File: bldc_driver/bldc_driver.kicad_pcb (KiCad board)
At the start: 2 copper layers, 46.4 x 26.5 mm, 81 parts, among them J1 I2C 1, J2 AVR-ISP-6, Q1 PSMN0R925YLC, Q2 PSMN0R925YLC, Q3 PSMN0R925YLC, Q4 PSMN0R925YLC, Q5 PSMN0R925YLC, Q6 PSMN0R925YLC, U1 ATmega328PB-AU, U2 INA199C2, U3 MIC4609

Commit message: added vias and things for grounding
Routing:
- net GND: vias 21 -> 53

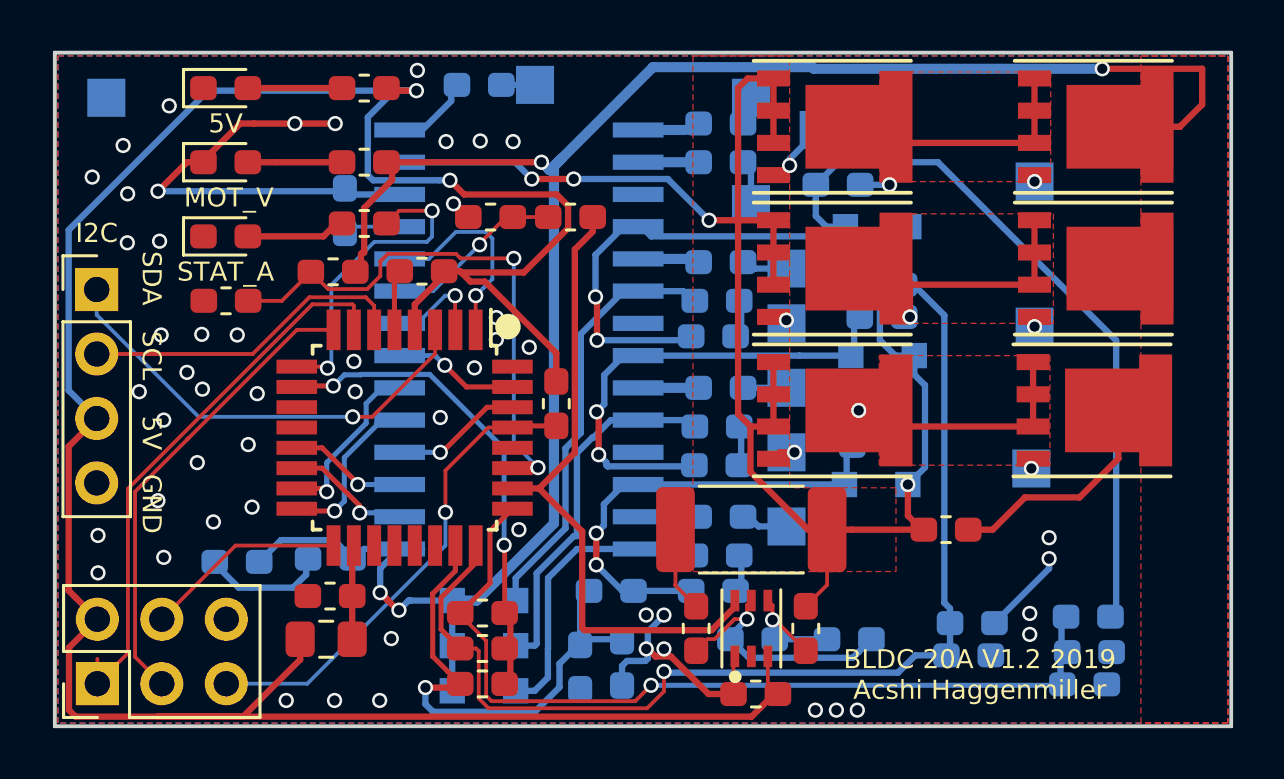
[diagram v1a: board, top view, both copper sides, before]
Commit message: redo of pcb for atmel micro at 5V to avoid emi problems resetting the old arm. initial conversion of code
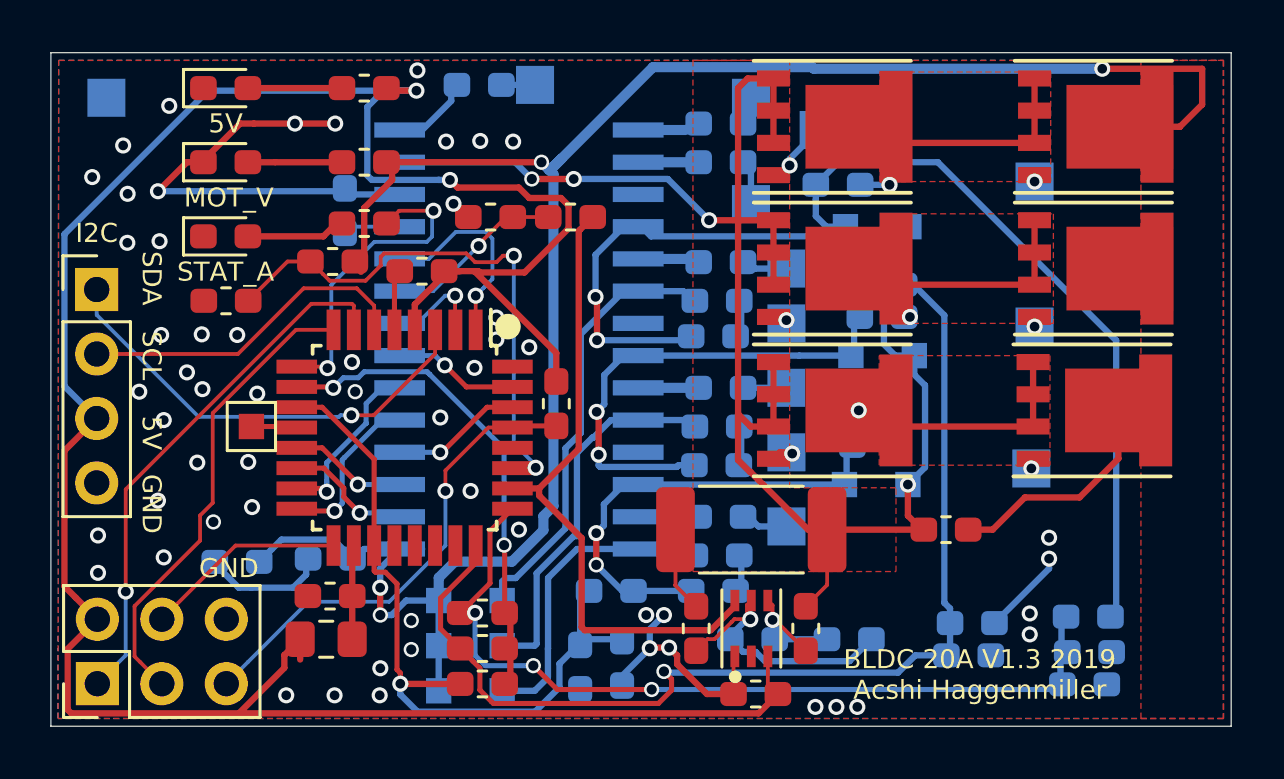
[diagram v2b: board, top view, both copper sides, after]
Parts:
- added REF**: TestPoint_Pad_1.5x1.5mm, TestPoint:TestPoint_Pad_1.5x1.5mm, F.Cu at (129.0, 87.1)
- moved D7 0.53 mm to (137.7, 94.0)
- moved D8 0.53 mm to (137.7, 95.8)
- moved D9 0.53 mm to (137.7, 97.5)
- moved R29 0.41 mm to (132.2, 80.6)
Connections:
- net /bldc_unit1/CURRENT renamed /CURRENT
- net /bldc_unit1/ENABLE renamed /ENABLE
- net /bldc_unit1/IN_HA renamed /HA
- net /bldc_unit1/IN_HB renamed /HB
- net /bldc_unit1/IN_HC renamed /HC
- net /bldc_unit1/IN_LA renamed /LA
- net /bldc_unit1/IN_LB renamed /LB
- net /bldc_unit1/IN_LC renamed /LC
- net /bldc_unit1/MOTOR_B renamed /MOTOR_B
- net /bldc_unit1/MOTOR_C renamed /MOTOR_C
- net /bldc_unit1/~FAULT renamed /~FAULT
- net Net-(R29-Pad2) renamed /V_MOT
- net Net-(U1-Pad22) renamed /TRIGGER2
- C17 pad 1: /bldc_unit1/MOTOR_A -> /MOTOR_A
- R23 pad 1: /bldc_unit1/MOTOR_A -> /MOTOR_A
- R26 pad 2: /bldc_unit1/MOTOR_A -> /MOTOR_A
- R5 pad 2: /bldc_unit1/MOTOR_A -> /MOTOR_A
- U1 pad 11: Net-(U1-Pad11) -> /MOTOR_A
- U1 pad 12: Net-(U1-Pad12) -> /TRIGGER
- U1 pad 19: Net-(U1-Pad19) -> /MOTOR_A
- U1 pad 23: /bldc_unit1/MOTOR_A -> Net-(U1-Pad23)
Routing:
- net /MOTOR_A: track 0.00 -> 29.7 mm, vias 0 -> 1
- net /bldc_unit1/MOTOR_A: track 20.2 -> 0.00 mm, vias 1 -> 0
- net /+5V: track 104.3 -> 102.0 mm
- net /TRIGGER: track 0.00 -> 1.86 mm
- net /MISO: track 22.5 -> 21.6 mm, vias 1 -> 2
- net /MOTOR_C: track 34.8 -> 34.1 mm, vias 1 -> 3
- net /bldc_unit1/MOTOR_SHUNT: track 66.7 -> 67.3 mm
- net GND: track 44.8 -> 44.3 mm, vias 53 -> 56
- net /+V_MOTOR: track 91.2 -> 91.7 mm
- net Net-(C15-Pad1): track 14.3 -> 14.9 mm
- net Net-(C14-Pad1): track 11.7 -> 12.2 mm
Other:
- board size 46.4 x 26.5 mm -> 46.5 x 26.5 mm
- net class Default: clearance 0.13 -> 0.15; via_dia 0.6 -> 0.635; via_drill 0.4 -> 0.381
- rule trace_clearance: 0.13 -> 0.15
- board text added: "BLDC 20A V1.3 2019 Acshi Haggenmiller"
- board text removed: "BLDC 20A V1.2 2019 Acshi Haggenmiller"

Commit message: fixed several vias that were still at the wrong size
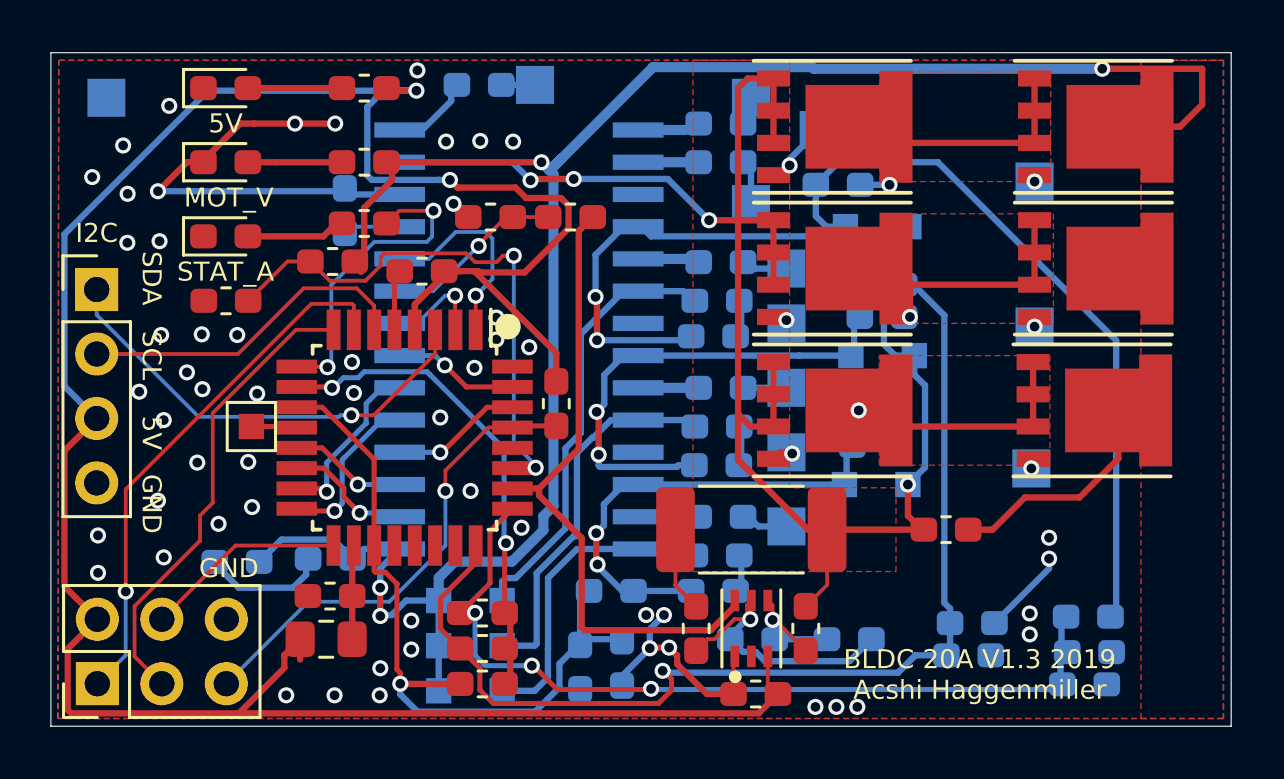
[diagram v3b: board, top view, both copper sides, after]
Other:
- rule via_min_drill: 0.3 -> 0.381
- rule via_min_size: 0.4 -> 0.635

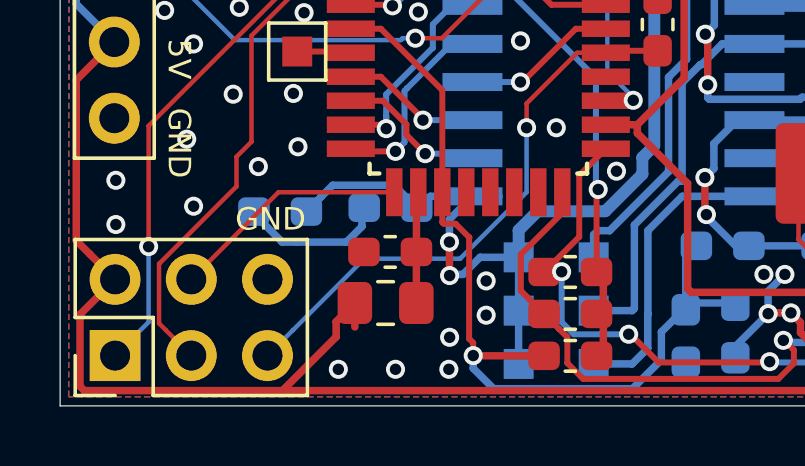
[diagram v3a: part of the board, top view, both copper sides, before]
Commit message: driver code working pretty well; some schematic changes started because we need more capacitance on the 5V rail.
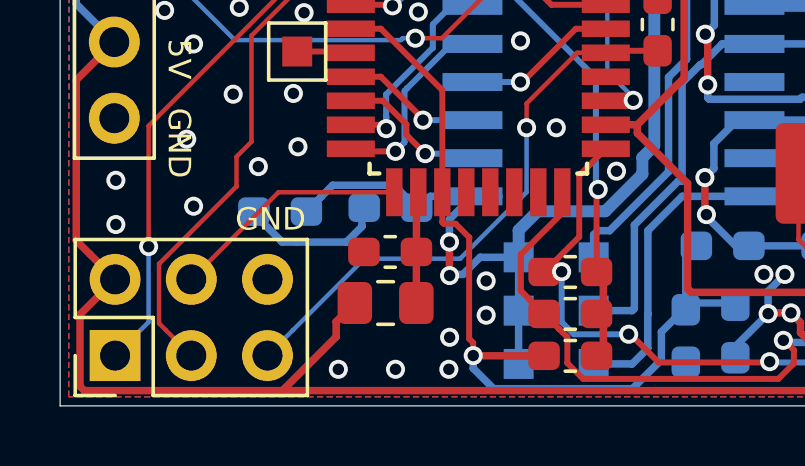
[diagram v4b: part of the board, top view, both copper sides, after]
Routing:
- net /+5V: track 102.0 -> 101.2 mm
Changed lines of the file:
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@@
-(kicad_pcb (version 20171130) (host pcbnew 5.0.2-bee76a0~70~ubuntu18.04.1)
+(kicad_pcb (version 20171130) (host pcbnew "(5.0.2)-1")
   (general
     (thickness 1.6)
     (drawings 28)
-    (tracks 699)
+    (tracks 698)
     (zones 0)
     (modules 82)
@@
   (segment (start 135.469 83.312) (end 135.469 82.312) (width 0.25) (layer F.Cu) (net 40))
   (segment (start 149.63 97.663) (end 149.855 97.663) (width 0.25) (layer F.Cu) (net 40))
-  (segment (start 130.9534 95.504) (end 130.9534 96.304) (width 0.25) (layer F.Cu) (net 40))
   (segment (start 133.597999 74.529601) (end 133.597999 77.228001) (width 0.25) (layer B.Cu) (net 40))
   (segment (start 133.597999 77.228001) (end 133.772997 77.402999) (width 0.25) (layer B.Cu) (net 40))

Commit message: bldc version 1.4 pcb
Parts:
- removed the C8 at (148.8, 95.5)
- removed the C9 at (152.6, 95.5)
- removed the D9 at (137.7, 97.5)
- removed the R10 at (150.9, 95.1)
- removed the R12 at (146.6, 95.1)
- removed the REF** at (150.1, 88.1)
- removed the REF** at (150.1, 91.1)
- removed the REF** at (159.9, 77.5)
- removed the REF** at (159.9, 83.2)
- removed the REF** at (159.8, 88.8)
- removed the REF** at (140.2, 73.7)
- removed the REF** at (151.4, 75.4)
- removed the REF** at (148.7, 74.2)
- removed the REF** at (148.7, 78.4)
- removed the REF** at (150.1, 80.9)
- removed the REF** at (150.1, 83.1)
- removed the REF** at (150.1, 85.6)
- added C3: 1uF, Capacitor_SMD:C_0603_1608Metric_Pad1.05x0.95mm_HandSolder, F.Cu at (126.4, 88.3)
- added C6: 100nF, Capacitor_SMD:C_0603_1608Metric_Pad1.05x0.95mm_HandSolder, F.Cu at (144.0, 95.1)
- added D6: DSS16UTR‎, Diode_SMD:D_SOD-323_HandSoldering, B.Cu at (137.7, 97.5)
- added G***: LOGO, Acshikh:Acshikh, B.Cu at (161.7, 83.5)
- added R7: 1k, Resistor_SMD:R_0603_1608Metric_Pad1.05x0.95mm_HandSolder, F.Cu at (146.4, 95.1)
- added REF**: TestPoint_Pad_1.5x1.5mm, TestPoint:TestPoint_Pad_1.5x1.5mm, F.Cu at (123.3, 74.2)
- added REF**: TestPoint_Pad_1.5x1.5mm, TestPoint:TestPoint_Pad_1.5x1.5mm, F.Cu at (140.6, 94.5)
- added REF**: TestPoint_Pad_1.5x1.5mm, TestPoint:TestPoint_Pad_1.5x1.5mm, F.Cu at (141.1, 89.6)
- added REF**: TestPoint_Pad_1.5x1.5mm, TestPoint:TestPoint_Pad_1.5x1.5mm, F.Cu at (135.7, 93.4)
- added REF**: TestPoint_Pad_1.5x1.5mm, TestPoint:TestPoint_Pad_1.5x1.5mm, F.Cu at (135.7, 95.0)
- added REF**: TestPoint_Pad_1.5x1.5mm, TestPoint:TestPoint_Pad_1.5x1.5mm, F.Cu at (135.7, 96.4)
- added REF**: TestPoint_Pad_1.5x1.5mm, TestPoint:TestPoint_Pad_1.5x1.5mm, F.Cu at (135.7, 97.8)
- C4: renamed from C2; value 100nF -> 1uF
- R16: renamed from R15; value 200R -> 10R
- R20: renamed from R16; value 200R -> 10R
- R23: renamed from R17; value 10R -> 1R
- R24: renamed from R18; value 10R -> 1R
- R25: renamed from R19; value 10R -> 1R
- R31: renamed from R11; value 2mR -> 4mR
- R9: renamed from R14; value 200R -> 10R
- U2: value INA199C2 -> INA199B1
- moved R19 0.18 mm to (147.4, 83.5)
- moved R12 0.16 mm to (147.5, 88.6)
- moved C11 0.15 mm to (147.5, 87.1)
- renumbered C17 to C10, C15 to C11, C18 to C12, C16 to C13, C19 to C14, C12 to C15, C7 to C16, C1 to C2, C11 to C5, C10 to C7, C13 to C8, C14 to C9, D7 to D4, D8 to D5, D4 to D7, D5 to D8, D6 to D9, Q5 to Q1, Q1 to Q2, Q2 to Q5, R23 to R10, R26 to R11, R21 to R12, R5 to R13, R6 to R14, R8 to R15, R24 to R17, R27 to R18, R22 to R19, R25 to R21, R28 to R22, R31 to R26, R32 to R27, R7 to R28, R9 to R29, R13 to R30, R33 to R4, R29 to R5, R30 to R6, R20 to R8
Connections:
- U1 pad 15: /LB -> /MOSI
- U1 pad 16: /LA -> /MISO
- U1 pad 17: /MOSI -> /SCK
- U1 pad 19: /MOTOR_A -> Net-(U1-Pad19)
- U1 pad 7: /MISO -> /LB
- U1 pad 8: /SCK -> /LA
- U2 pad 4: Net-(C8-Pad2) -> /bldc_unit1/MOTOR_SHUNT
- U2 pad 5: Net-(C8-Pad1) -> GND
- U2 pad 6: /CURRENT -> Net-(R7-Pad2)
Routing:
- net /+5V: track 101.2 -> 40.9 mm, vias 2 -> 5
- net GND: track 44.3 -> 77.2 mm, vias 56 -> 21
- net /bldc_unit1/GLB: track 2.44 -> 22.8 mm, vias 1 -> 2
- net /bldc_unit1/GLA: track 2.78 -> 22.5 mm, vias 1 -> 2
- net /bldc_unit1/GHA: track 2.30 -> 15.8 mm, vias 1 -> 2
- net /bldc_unit1/GHB: track 2.12 -> 15.6 mm, vias 1 -> 2
- net /bldc_unit1/GHC: track 2.10 -> 15.0 mm, vias 1 -> 2
- net Net-(C8-Pad1): track 10.7 -> 0.00 mm, vias 1 -> 0
- net /MOTOR_A: track 29.7 -> 39.4 mm, vias 1 -> 2
- net /bldc_unit1/GLC: track 4.14 -> 13.7 mm, vias 1 -> 2
- net /MISO: track 21.6 -> 12.2 mm, vias 2 -> 0
- net /SCK: track 18.5 -> 9.95 mm
- net Net-(C8-Pad2): track 5.64 -> 0.00 mm, vias 1 -> 0
- net /MOTOR_B: track 42.3 -> 46.6 mm
- net /bldc_unit1/MOTOR_SHUNT: track 67.3 -> 71.3 mm, vias 4 -> 19
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- added copper zone on In2.Cu, net /+5V
- added copper zone on B.Cu, net /+V_MOTOR
- added copper zone on In1.Cu, net /+V_MOTOR
- added copper zone on In2.Cu, net /+V_MOTOR
- added copper zone on In1.Cu, net /bldc_unit1/MOTOR_SHUNT
- added copper zone on In2.Cu, net /bldc_unit1/MOTOR_SHUNT
- added copper zone on In1.Cu, net GND
- added copper zone on In2.Cu, net GND
- removed copper zone on B.Cu, net GND
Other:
- copper layers 2 -> 4
- rule pad_to_mask_clearance: 0.06 -> 0.05
- rule solder_mask_min_width: 0.25 -> 0.15
- board text added: "BLDC 20A V1.4 2020 Acshi Haggenmiller"
- board text added: "JLCJLCJLCJLC"
- board text removed: "1"
- board text removed: "2"
- board text removed: "3"
- board text removed: "4"
- board text removed: "5"
- board text removed: "6"
- board text removed: "BLDC 20A V1.3 2019 Acshi Haggenmiller"
